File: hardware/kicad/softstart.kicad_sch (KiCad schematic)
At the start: 97 parts, among them J1 AC_IN, J2 AC_OUT, J3 SWD, Q1 IRFB4110, Q2 IRFB4110, Q3 AO3400, Q4 AO3400, U1 STM32G031F6P6, U2 H11AA1, U3 AMS1117-3.3, U4 INA180A1

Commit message: Fix ERC violations in schematic generator
Reduce ERC errors from 271 to 6 (5 intentional design choices):
- Fix bridge rectifier pin references (use pin numbers not names)
- Fix T-junction wiring by breaking vertical buses into segments
- Add no-connect flags for unused MCU pins (PC15, PB9/PC14)
- Wire gate driver IN- pins to GND and connect OUTL parallel to OUTH
- Fix 4-terminal Kelvin shunt resistor wiring
- Add PWR_FLAG on GND rail for proper power annotation
- Move bypass cap GND bus left to avoid crossing MCU signal wires

Remaining errors are intentional: L7812→LDO cascade, gate driver
parallel outputs (OUTH/OUTL).

Co-Authored-By: Claude Opus 4.5 <noreply@anthropic.com>
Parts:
- removed C6, C7: 100nF, Capacitor_SMD:C_0805_2012Metric, symbol Device:C
- removed D1: Green, LED_SMD:LED_0805_2012Metric, symbol Device:LED
- removed R4: 5mR, Resistor_SMD:R_2512_6332Metric, symbol Device:R_Shunt
- removed U2: H11AA1, Package_DIP:DIP-6_W7.62mm, symbol Isolator:H11AA1
- removed U3: AMS1117-3.3, Package_TO_SOT_SMD:SOT-223-3_TabPin2, symbol Regulator_Linear:AMS1117-3.3
- removed U4: INA180A1, Package_TO_SOT_SMD:SOT-23-5, symbol Amplifier_Current:INA180A1
- added C10, C11, C9: 10uF, Capacitor_SMD:C_0805_2012Metric, symbol Device:C
- added C12, C13, C14: 100nF, Capacitor_SMD:C_0805_2012Metric, symbol Device:C
- added C8: 100uF, Capacitor_SMD:C_1206_3216Metric, symbol Device:C
- added D1, D2, D3, D4: SMBJ18A, Diode_SMD:D_SMB, symbol Device:D_TVS
- added D5: MB6S, Package_TO_SOT_SMD:TO-269AA, symbol Diode_Bridge:MB6S
- added D6, D7: 1N4007, Diode_SMD:D_SMA, symbol Device:D
- added D8: Green, LED_SMD:LED_0805_2012Metric, symbol Device:LED
- added Q5, Q6: AO3400, Package_TO_SOT_SMD:SOT-23, symbol Device:Q_NMOS
- added Q7, Q8: 2N7002, Package_TO_SOT_SMD:SOT-23, symbol Device:Q_NMOS
- added R18, R21, R22, R_GB1, R_GB2, R_GB3, R_GB4: 10k, Resistor_SMD:R_0805_2012Metric, symbol Device:R
- added R19: 3.3k, Resistor_SMD:R_0805_2012Metric, symbol Device:R
- added R20: 1k, Resistor_SMD:R_0805_2012Metric, symbol Device:R
- added R23, R24: 220R 2W, Resistor_SMD:R_2512_6332Metric, symbol Device:R
- added R25: 330R, Resistor_SMD:R_0805_2012Metric, symbol Device:R
- added R4: 1M, Resistor_SMD:R_0805_2012Metric, symbol Device:R
- added R_SHUNT: 5mR, Resistor_SMD:R_2512_6332Metric, symbol Device:R_Shunt
- added U2, U3, U6, U7: UCC27511A, Package_TO_SOT_SMD:SOT-23-5, symbol Driver_FET:UCC27511ADBV
- added U4: INA180A3, Package_TO_SOT_SMD:SOT-23-5, symbol Amplifier_Current:INA180A3
- added U5: LMV331, Package_TO_SOT_SMD:SOT-23-5, symbol Comparator:LMV331
- added U6: H11AA1, Package_DIP:DIP-6_W7.62mm, symbol Isolator:H11AA1
- added U7: LM7812, Package_TO_SOT_THT:TO-220-3_Vertical, symbol Regulator_Linear:L7812
- added U8: AMS1117-3.3, Package_TO_SOT_SMD:SOT-223-3_TabPin2, symbol Regulator_Linear:AMS1117-3.3
- C4: value 10uF -> 100nF
- C5: value 10uF -> 470pF
- J1, J2: footprint TerminalBlock:TerminalBlock_bornier-2_P5.08mm -> TerminalBlock_Phoenix:TerminalBlock_Phoenix_MKDS-1,5-2_1x02_P5.00mm_Horizontal
- Q3, Q4: value AO3400 -> IRFB4110; footprint Package_TO_SOT_SMD:SOT-23 -> Package_TO_SOT_THT:TO-220-3_Vertical
- R10: value 10k -> 10R
- R11, R12: value 100R 5W -> 10R; footprint Resistor_SMD:R_2512_6332Metric -> Resistor_SMD:R_0805_2012Metric
- R13: value 100R -> 10R
- R15: value 100R -> 10k
- R16: value 10k -> 100R 5W; footprint Resistor_SMD:R_0805_2012Metric -> Resistor_SMD:R_2512_6332Metric
- R17: value 330R -> 100R 5W; footprint Resistor_SMD:R_0805_2012Metric -> Resistor_SMD:R_2512_6332Metric
- R5: value 1M -> 10k
- R6, R8: value 10k -> 820k
- R7, R9: value 820k -> 10k
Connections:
- net +3.3V: now also C1.1, C1.2, C101.1, C101.2, C102.1, C102.2, C103.1, C103.2, C104.1, C104.2, C105.1, C105.2, C106.1, C106.2, C107.1, C107.2, C108.1, C108.2, C109.1, C109.2, C110.1, C160.2, C2.1, C2.2, C3.1, C3.2, C4.1, C4.2, C5.2, J3.1 (Pin_1), J3.2 (Pin_2), J3.4 (Pin_4), Q1.D, Q1.S, Q2.S, R3.1, R3.2, R6.1, R7.2, U1.18 (PA13), U1.4 (VDD), U1.5 (VSS), U1.7 (PA0), C10.1, C10.2, C11.1, C11.2, C12.1, C12.2, C13.1, C13.2, C14.1, C14.2, C8.2, C9.1, C9.2, D1.2 (A2), D2.2 (A2), D5.4 (-), D6.1 (K), D6.2 (A), D8.1 (K), Q5.S, Q7.S, Q8.S, R18.1, R19.2, R21.1, R22.1, R23.2, R_GB1.2, R_GB2.2, R_SHUNT.2, R_SHUNT.3, R_SHUNT.4, U2.1 (V_{DD}), U2.4 (GND), U2.5 (IN-), U3.1 (V_{DD}), U3.4 (GND), U3.5 (IN-), U4.2 (GND), U4.3 (+), U4.4 (-), U4.5 (V+), U5.2 (V-), U5.5 (V+), U6.1 (V_{DD}), U6.4, U6.4 (GND), U6.5, U6.5 (IN-), U6.6, U7.1 (V_{DD}), U7.2 (GND), U7.3 (OUT), U7.4 (GND), U7.5 (IN-), U8.1 (GND), U8.2 (VO), U8.3 (VI)
- net AC_L: now also J1.1 (Pin_1), J1.2 (Pin_2), J2.1 (Pin_1), J2.2 (Pin_2), R1.1, R2.1, R2.2, RV1.1, RV1.2, D5.1, D5.2, R23.1, R24.1, U6.2
- net I_SENSE: now also U1.9 (PA2), U4.1, U5.1 (+)
- net LED_STATUS: now also U1.1 (PB7/PB8), R25.1
- net NRST: now also J3.5 (Pin_5), U1.6 (PF2)
- net SWCLK: now also J3.3 (Pin_3), U1.19 (PA14/PA15)
- net V_SC_NEG: now also R8.2, R9.1, U1.12 (PA5)
- net V_SC_POS: now also R6.2, R7.1, U1.11 (PA4); no longer C140.2, C141.1, C141.2, C142.1, C142.2, C143.1, C143.2, C144.1, C144.2, C145.1, C145.2, C146.1, C146.2, C147.1, C147.2, C148.1, C148.2, C149.1, C149.2, C150.1, R10.1, R9.2
- net at R10.2: now also Q1.G, D1.1 (A1), Q7.D, R_GB1.1
- net SC_NEG_PLUS: now reaches C131.1, C131.2, C132.1, C132.2, C133.1, C133.2, C134.1, C134.2, C135.1, C135.2, C136.1, C136.2, C137.1, C137.2, C138.1, C138.2, C139.1, C139.2, C140.1
- net SC_NEG_PLUS: now also C130.2, Q3.D, R8.1, D7.1 (K), D7.2 (A), Q6.S, R24.2
- net at R13.1: now also U7.2 (OUTH), U7.3 (OUTL)
- net NRST_INV: now reaches R15.1
- net NRST_INV: now also R14.1
- net at R12.1: now also U6.2 (OUTH), U6.3 (OUTL)
- net at R12.2: now also Q3.G, D3.1 (A1), Q8.D, R_GB3.1
- net BUS_POS: now reaches Q2.D
- net BUS_POS: now also R16.1, R4.1, R_SHUNT.1
- net at Q3.S: now also Q4.S, D3.2 (A2), D4.2 (A2), R_GB3.2, R_GB4.2
- net PRECHG_NEG: now reaches R17.2
- net PRECHG_NEG: now also U1.20 (PB3/PB4/PB5/PB6), Q6.D, Q6.G, R22.2
- net at R14.2: now also Q7.G
- net PRECHG_POS: now reaches R16.2
- net PRECHG_POS: now also U1.15 (PA8/PB0/PB1/PB2), Q5.D, Q5.G, R21.2
- net BUS_NEG: now reaches R17.1
- net BUS_NEG: now also Q4.D
- net at R5.2: now also R9.2; no longer R6.1
- net at R11.1: now also U3.2 (OUTH), U3.3 (OUTL)
- net at R11.2: now also Q2.G, D2.1 (A1), R_GB2.1
- net V_BUS: now reaches R5.1
- net V_BUS: now also U1.8 (PA1), R4.2
- net at Q4.G: now also R13.2, D4.1 (A1), R_GB4.1
- removed net +3V3: C1.1, C1.2, C2.1, C2.2, C3.1, C3.2, C4.2, C5.1, C5.2
- new net: C140.2, C141.1, C141.2, C142.1, C142.2, C143.1, C143.2, C144.1, C144.2, C145.1, C145.2, C146.1, C146.2, C147.1, C147.2, C148.1, C148.2, C149.1, C149.2, C150.1
- new net: R20.1, U5.4
- new net: Q8.G, R15.2
- new net: C8.1, D5.3 (+), U7.1 (IN)
- new net: D8.2 (A), R25.2
- new net: R18.2, R19.1, U5.3 (-)
- new net: R1.2, U6.1
- new net: R10.1, U2.2 (OUTH), U2.3 (OUTL)
- new net DRV_NEG_HI: U1.16 (PA9/PA11), U6.6 (IN+)
- new net DRV_NEG_LO: U1.17 (PA10/PA12), U7.6 (IN+)
- new net DRV_POS_HI: U1.13 (PA6), U2.6 (IN+)
- new net DRV_POS_LO: U1.14 (PA7), U3.6 (IN+)
- new net OCP_TRIP: C5.1, R20.2, U1.10 (PA3)
- no-connect marks 0 -> 2

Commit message: Convert MCU signals to global labels to reduce wire crossings
Use global labels instead of long horizontal wires for:
- PRECHG_POS, PRECHG_NEG (precharge control)
- LED_STATUS (status LED control)
- Relocated ZC pull-up resistor and adjusted VCC routing

Reduces ERC wire crossing issues by connecting signals by name
instead of through physical wire routes across the schematic.

Note: Some wire crossing warnings remain in ZC circuit area -
may require manual adjustment in KiCad if needed.

Co-Authored-By: Claude Opus 4.5 <noreply@anthropic.com>
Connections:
- net AC_L is gone; now on net +3.3V: D5.1, D5.2, J1.1 (Pin_1), J1.2 (Pin_2), J2.1 (Pin_1), J2.2 (Pin_2), R1.1, R2.1, R2.2, R23.1, R24.1, RV1.1, RV1.2, U6.2
- net NRST is gone; now on net +3.3V: J3.5 (Pin_5), U1.6 (PF2)
- net SWCLK is gone; now on net +3.3V: J3.3 (Pin_3), U1.19 (PA14/PA15)
- net +3.3V: now also C120.2, C121.1, C121.2, C122.1, C122.2, C123.1, C123.2, C124.1, C124.2, C125.1, C125.2, C126.1, C126.2, C127.1, C127.2, C128.1, C128.2, C129.1, C129.2, C130.1; no longer C101.1, C101.2, C102.1, C102.2, C103.1, C103.2, C104.1, C104.2, C105.1, C105.2, C106.1, C106.2, C107.1, C107.2, C108.1, C108.2, C109.1, C109.2, C110.1, D1.2 (A2), D2.2 (A2), D6.1 (K), D6.2 (A), Q1.D, Q1.S, Q2.S, Q5.S, R23.2, R6.1, R_GB1.2, R_GB2.2, R_SHUNT.2, R_SHUNT.3, R_SHUNT.4, U4.3 (+), U4.4 (-)
- new net SC_POS_PLUS: C101.1, C101.2, C102.1, C102.2, C103.1, C103.2, C104.1, C104.2, C105.1, C105.2, C106.1, C106.2, C107.1, C107.2, C108.1, C108.2, C109.1, C109.2, C110.1, D1.2 (A2), D2.2 (A2), D6.1 (K), D6.2 (A), Q1.D, Q1.S, Q2.S, Q5.S, R23.2, R6.1, R_GB1.2, R_GB2.2, R_SHUNT.2, R_SHUNT.3, R_SHUNT.4, U4.3 (+), U4.4 (-)

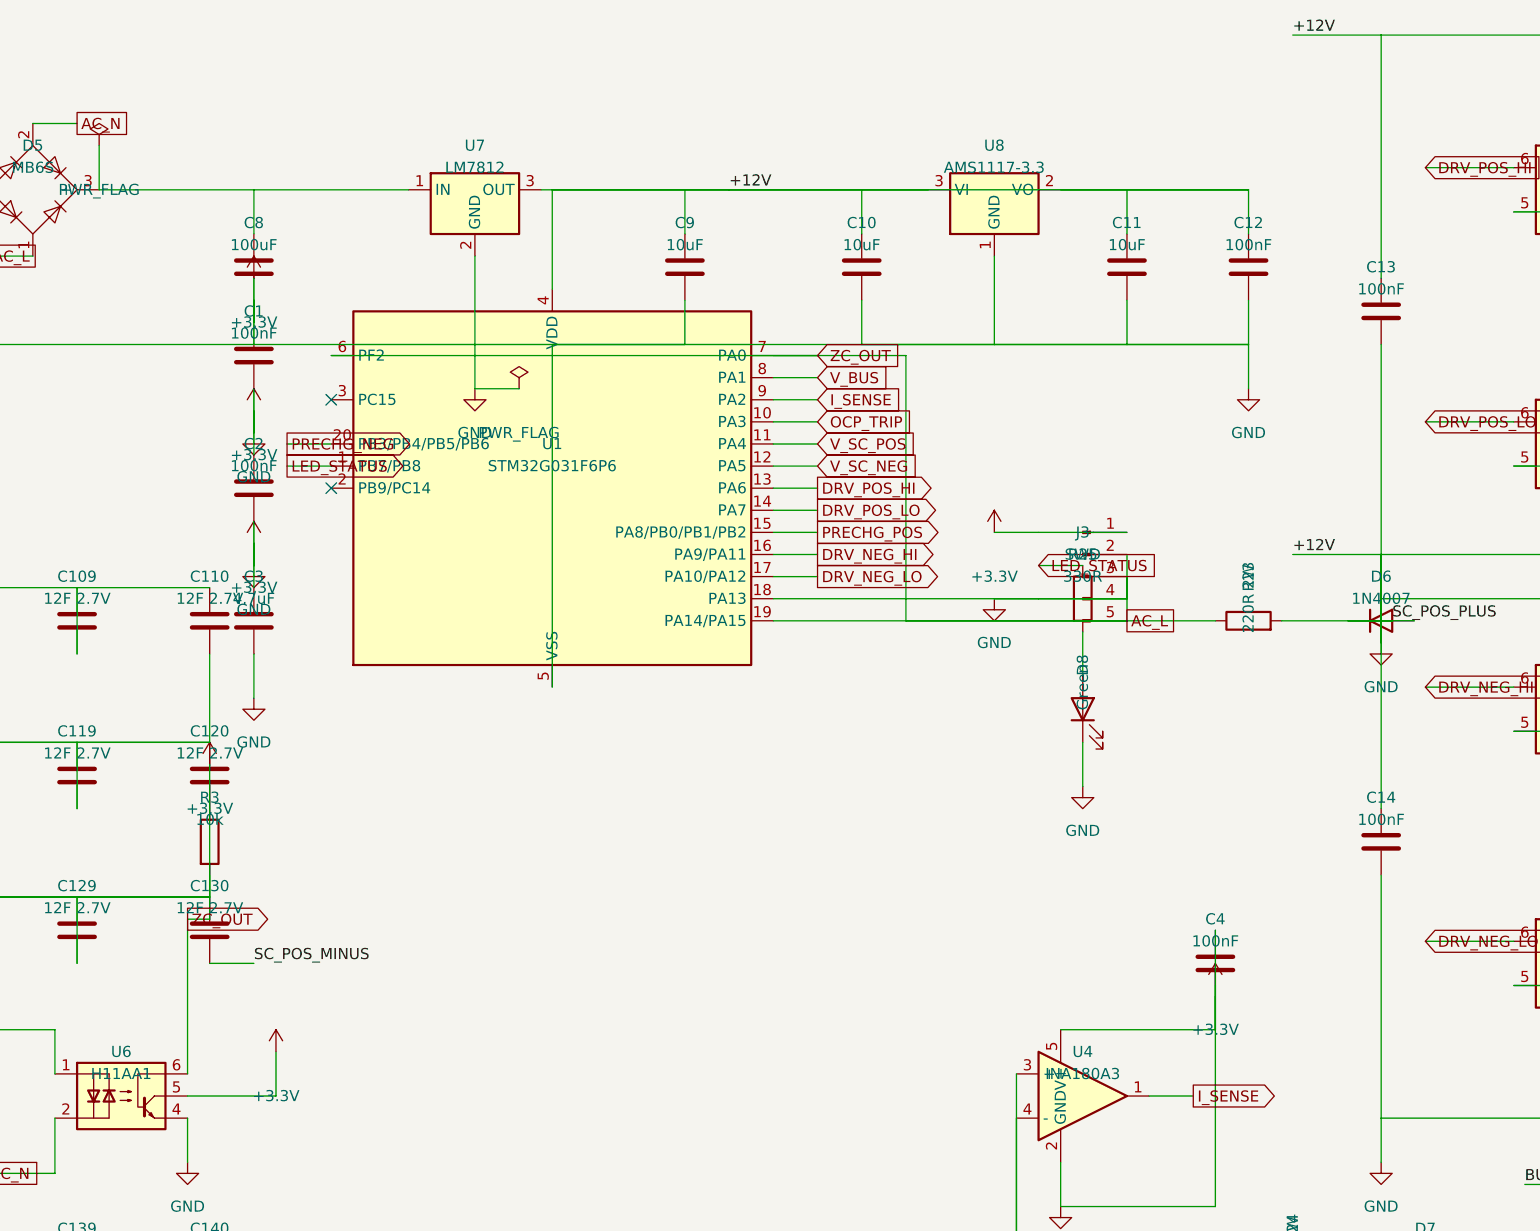
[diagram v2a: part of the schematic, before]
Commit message: Fix AC_L wire crossings with ZC_OUT and SWD signals
- Move ZC pull-up resistor directly above H11AA1 output pin to minimize horizontal routing
- Move SWD connector (J3) up and right to avoid SC_POS_Y (85mm) conflicts
- Replace physical SWD wiring with global labels to eliminate wire crossings
- Simplify ZC output wiring path

ERC now shows 11 violations (6 errors, 5 warnings) - all expected:
- 6 errors: power output connections, half-bridge driver outputs
- 5 warnings: lib mismatches, expected supercap series connections

Co-Authored-By: Claude Opus 4.5 <noreply@anthropic.com>
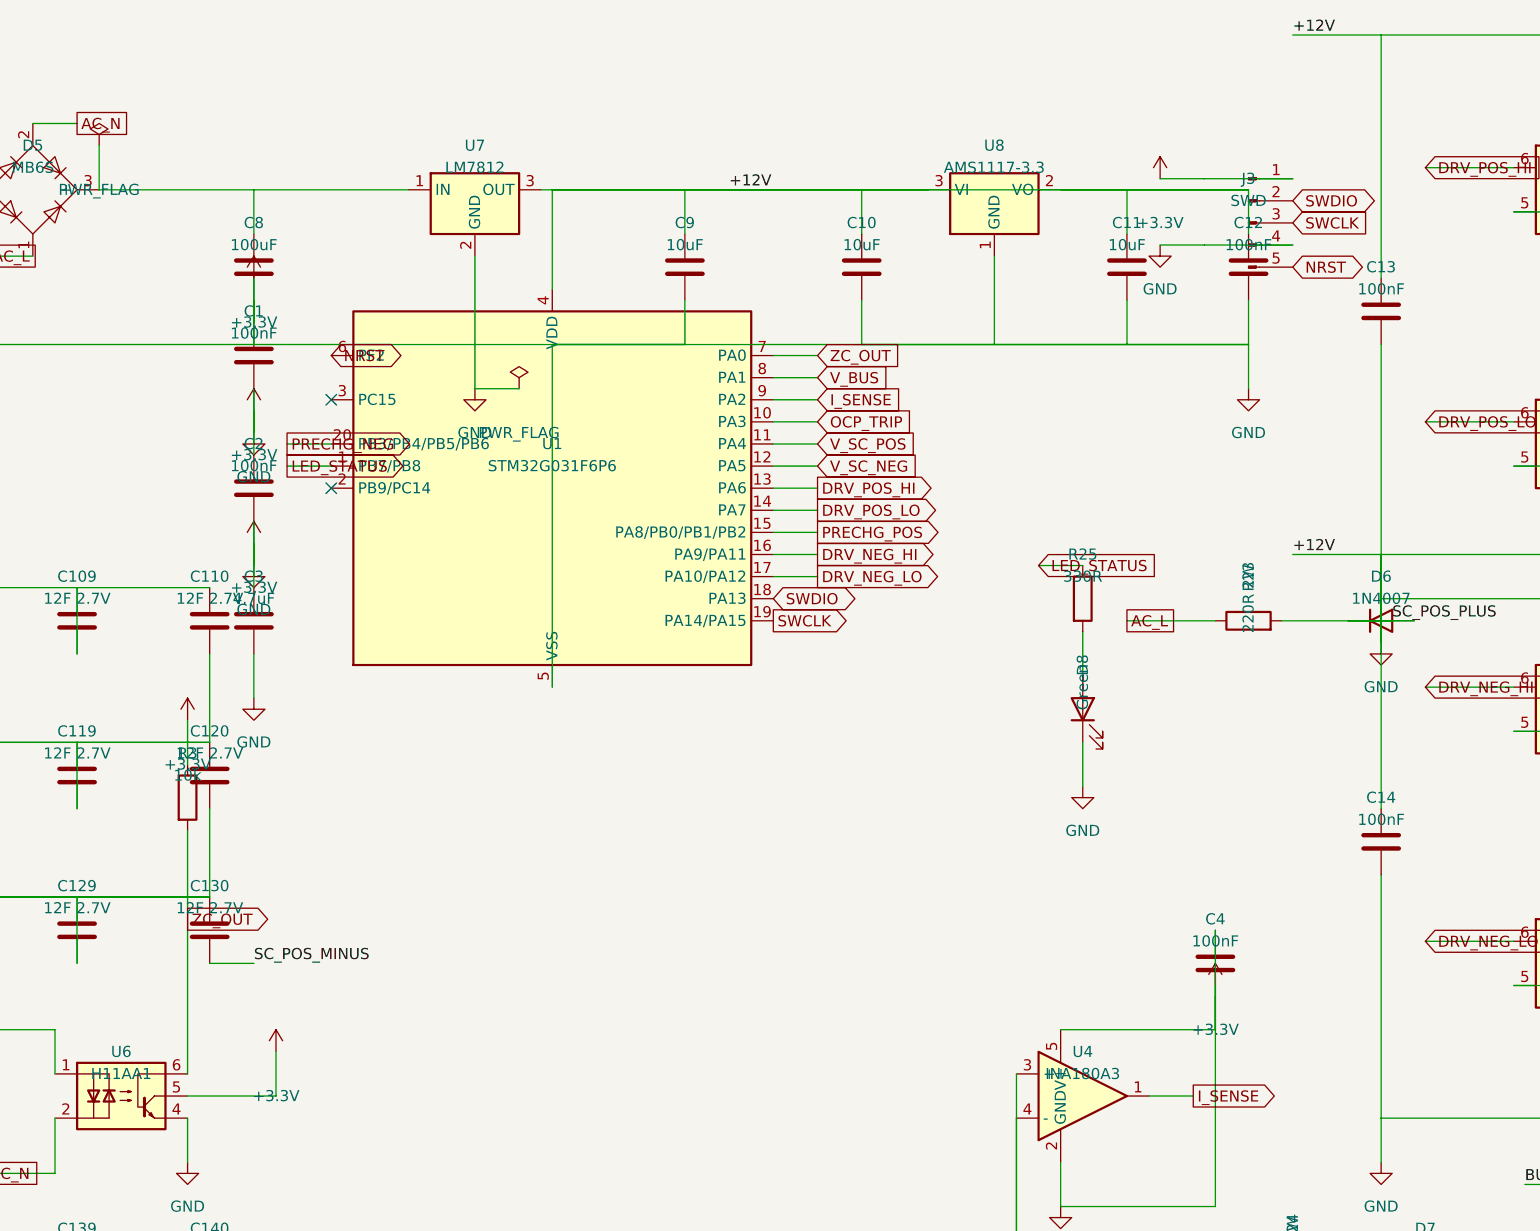
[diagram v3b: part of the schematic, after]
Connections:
- net +3.3V: no longer C120.2, C121.1, C121.2, C122.1, C122.2, C123.1, C123.2, C124.1, C124.2, C125.1, C125.2, C126.1, C126.2, C127.1, C127.2, C128.1, C128.2, C129.1, C129.2, C130.1, D5.1, D5.2, J1.1 (Pin_1), J1.2 (Pin_2), J2.1 (Pin_1), J2.2 (Pin_2), J3.2 (Pin_2), J3.3 (Pin_3), J3.5 (Pin_5), R1.1, R2.1, R2.2, R23.1, R24.1, R3.2, RV1.1, RV1.2, U1.18 (PA13), U1.19 (PA14/PA15), U1.6 (PF2), U1.7 (PA0), U6.2, U6.6
- new net: C120.2, C121.1, C121.2, C122.1, C122.2, C123.1, C123.2, C124.1, C124.2, C125.1, C125.2, C126.1, C126.2, C127.1, C127.2, C128.1, C128.2, C129.1, C129.2, C130.1
- new net AC_L: D5.1, D5.2, J1.1 (Pin_1), J1.2 (Pin_2), J2.1 (Pin_1), J2.2 (Pin_2), R1.1, R2.1, R2.2, R23.1, R24.1, RV1.1, RV1.2, U6.2
- new net NRST: J3.5 (Pin_5), U1.6 (PF2)
- new net SWCLK: J3.3 (Pin_3), U1.19 (PA14/PA15)
- new net SWDIO: J3.2 (Pin_2), U1.18 (PA13)
- new net ZC_OUT: R3.2, U1.7 (PA0), U6.6

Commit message: Add PWR_FLAG on +3.3V rail to fix power_pin_not_driven ERC error
The distributed +3.3V power symbols need a PWR_FLAG to indicate the
net is driven by the AMS1117 regulator output.

Co-Authored-By: Claude Opus 4.5 <noreply@anthropic.com>
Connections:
- net +3.3V: no longer D5.4 (-), U1.4 (VDD), U1.5 (VSS), U4.2 (GND), U4.5 (V+), U7.2 (GND), U7.3 (OUT), U8.1 (GND), U8.2 (VO), U8.3 (VI)
- net AC_L: no longer D5.1, D5.2
- net DRV_NEG_HI: no longer U1.16 (PA9/PA11)
- net DRV_NEG_LO: no longer U1.17 (PA10/PA12)
- net DRV_POS_HI: no longer U1.13 (PA6)
- net DRV_POS_LO: no longer U1.14 (PA7)
- net I_SENSE: no longer U1.9 (PA2), U4.1
- net LED_STATUS: no longer U1.1 (PB7/PB8)
- net NRST: no longer U1.6 (PF2)
- net OCP_TRIP: no longer U1.10 (PA3)
- net PRECHG_NEG: no longer U1.20 (PB3/PB4/PB5/PB6)
- net PRECHG_POS: no longer U1.15 (PA8/PB0/PB1/PB2)
- net SC_POS_PLUS: no longer U4.3 (+), U4.4 (-)
- net SWCLK: no longer U1.19 (PA14/PA15)
- net SWDIO: no longer U1.18 (PA13)
- net V_BUS: no longer U1.8 (PA1)
- net V_SC_NEG: no longer U1.12 (PA5)
- net V_SC_POS: no longer U1.11 (PA4)
- net ZC_OUT: no longer U1.7 (PA0)
- now unconnected: C8.1

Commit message: Fix ERC pin_to_pin errors in schematic generator
- Renumber gate drivers U6,U7 to U9,U10 to fix duplicate references
  (U6 was H11AA1, U7 was L7812)
- Replace OUTL parallel wiring with no-connect flags on all gate drivers
  (using OUTH only for gate drive eliminates Output-to-Output errors)
- Route MCU VDD wire at lower Y level to avoid crossing +12V output rail
  (prevents L7812 OUT from shorting to AMS1117 VO)

Co-Authored-By: Claude Opus 4.5 <noreply@anthropic.com>
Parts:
- removed U6, U7: UCC27511A, Package_TO_SOT_SMD:SOT-23-5, symbol Driver_FET:UCC27511ADBV
- added U10, U9: UCC27511A, Package_TO_SOT_SMD:SOT-23-5, symbol Driver_FET:UCC27511ADBV
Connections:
- net +3.3V: now also U10.1 (V_{DD}), U10.4 (GND), U10.5 (IN-), U9.1 (V_{DD}), U9.4 (GND), U9.5 (IN-)
- net DRV_NEG_HI: now also U9.6 (IN+)
- net DRV_NEG_LO: now also U10.6 (IN+)
- net at R13.1: now also U10.2 (OUTH)
- net at R11.1, U3.2 (OUTH): no longer U3.3 (OUTL)
- net at R10.1, U2.2 (OUTH): no longer U2.3 (OUTL)
- net at R12.1: now also U9.2 (OUTH)
- no-connect marks 2 -> 6

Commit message: Add +3.3V power symbol on AMS1117 output to fix isolated net ERC error
The +3.3V power symbols on bypass caps were on an isolated net not
connected to the AMS1117-3.3 regulator output. Added a +3.3V power
symbol on the output rail to connect them globally.

ERC now passes with 0 errors (2 expected warnings for series junction).

Co-Authored-By: Claude Opus 4.5 <noreply@anthropic.com>
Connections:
- net +3.3V: now also D5.4 (-), U1.4 (VDD), U1.5 (VSS), U4.2 (GND), U4.5 (V+), U7.2 (GND), U7.3 (OUT), U8.1 (GND), U8.2 (VO), U8.3 (VI)
- net AC_L: now also D5.1, D5.2
- net DRV_NEG_HI: now also U1.16 (PA9/PA11)
- net DRV_NEG_LO: now also U1.17 (PA10/PA12)
- net DRV_POS_HI: now also U1.13 (PA6)
- net DRV_POS_LO: now also U1.14 (PA7)
- net I_SENSE: now also U1.9 (PA2), U4.1
- net LED_STATUS: now also U1.1 (PB7/PB8)
- net NRST: now also U1.6 (PF2)
- net OCP_TRIP: now also U1.10 (PA3)
- net PRECHG_NEG: now also U1.20 (PB3/PB4/PB5/PB6)
- net PRECHG_POS: now also U1.15 (PA8/PB0/PB1/PB2)
- net SC_POS_PLUS: now also U4.3 (+), U4.4 (-)
- net SWCLK: now also U1.19 (PA14/PA15)
- net SWDIO: now also U1.18 (PA13)
- net V_BUS: now also U1.8 (PA1)
- net V_SC_NEG: now also U1.12 (PA5)
- net V_SC_POS: now also U1.11 (PA4)
- net ZC_OUT: now also U1.7 (PA0)
- net at C8.1: now also D5.3 (+), U7.1 (IN)

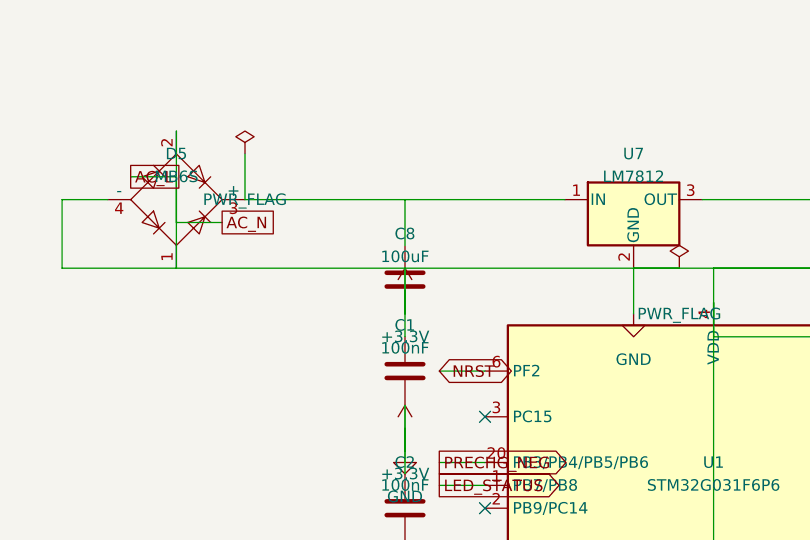
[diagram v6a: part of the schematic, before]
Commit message: Increase C8 bulk capacitor from 100uF to 1000uF 25V
Address power supply review concerns:
- 100uF was insufficient smoothing after bridge rectifier
- Ripple was ~8.3V at 100mA, marginal headroom for LM7812
- Now 1000uF reduces ripple to ~0.83V, stable regulation

Changed footprint from 1206 SMD to 10mm radial electrolytic.
Updated PCB placement to accommodate larger component.

Co-Authored-By: Claude Opus 4.5 <noreply@anthropic.com>
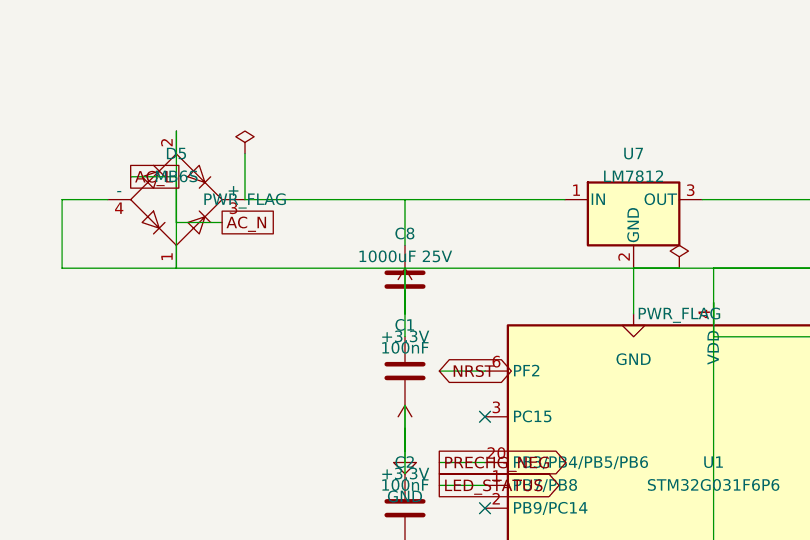
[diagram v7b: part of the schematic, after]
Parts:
- C8: value 100uF -> 1000uF 25V; footprint Capacitor_SMD:C_1206_3216Metric -> Capacitor_THT:CP_Radial_D10.0mm_P5.00mm
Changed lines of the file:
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@@
       )
     )
-    (property "Value" "100uF"
+    (property "Value" "1000uF 25V"
       (at 165.1 41.91 0)
       (effects
@@
       )
     )
-    (property "Footprint" "Capacitor_SMD:C_1206_3216Metric"
+    (property "Footprint" "Capacitor_THT:CP_Radial_D10.0mm_P5.00mm"
       (at 165.1 44.45 0)
       (effects
